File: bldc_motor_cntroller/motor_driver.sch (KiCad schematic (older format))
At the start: 44 parts

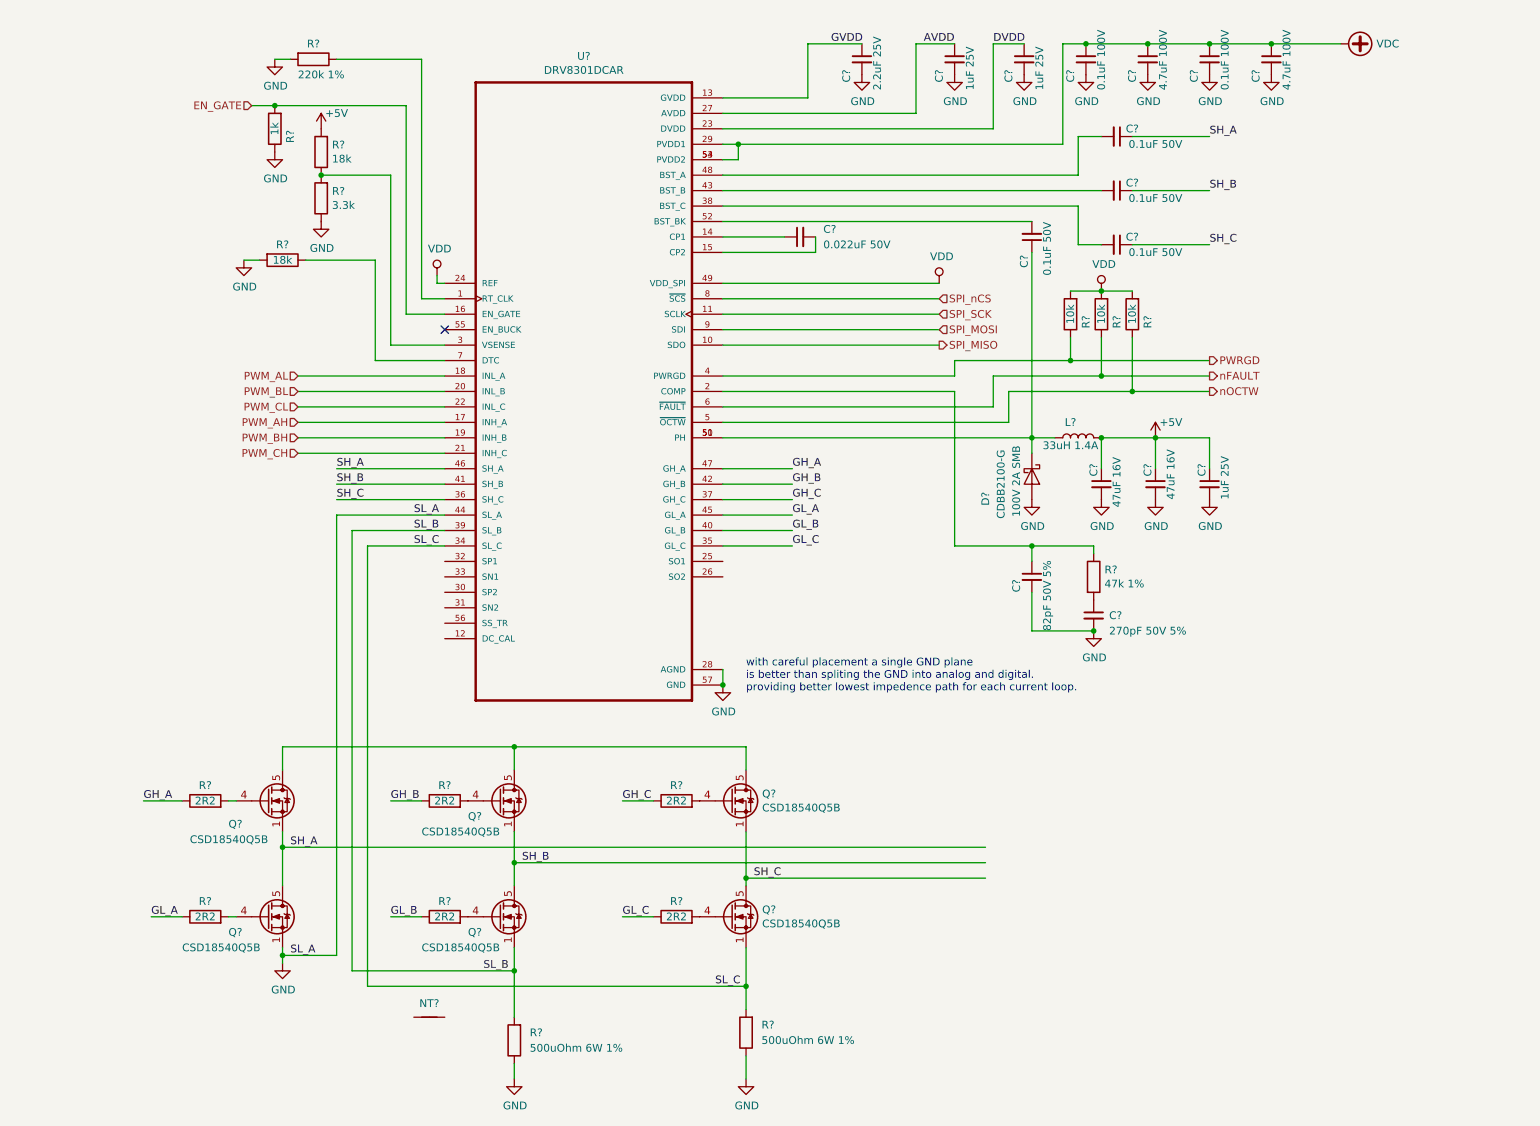
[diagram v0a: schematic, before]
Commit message: finished motor driver interface.
Signed-off-by: azmat bilal <azmat.bilal@outlook.com>
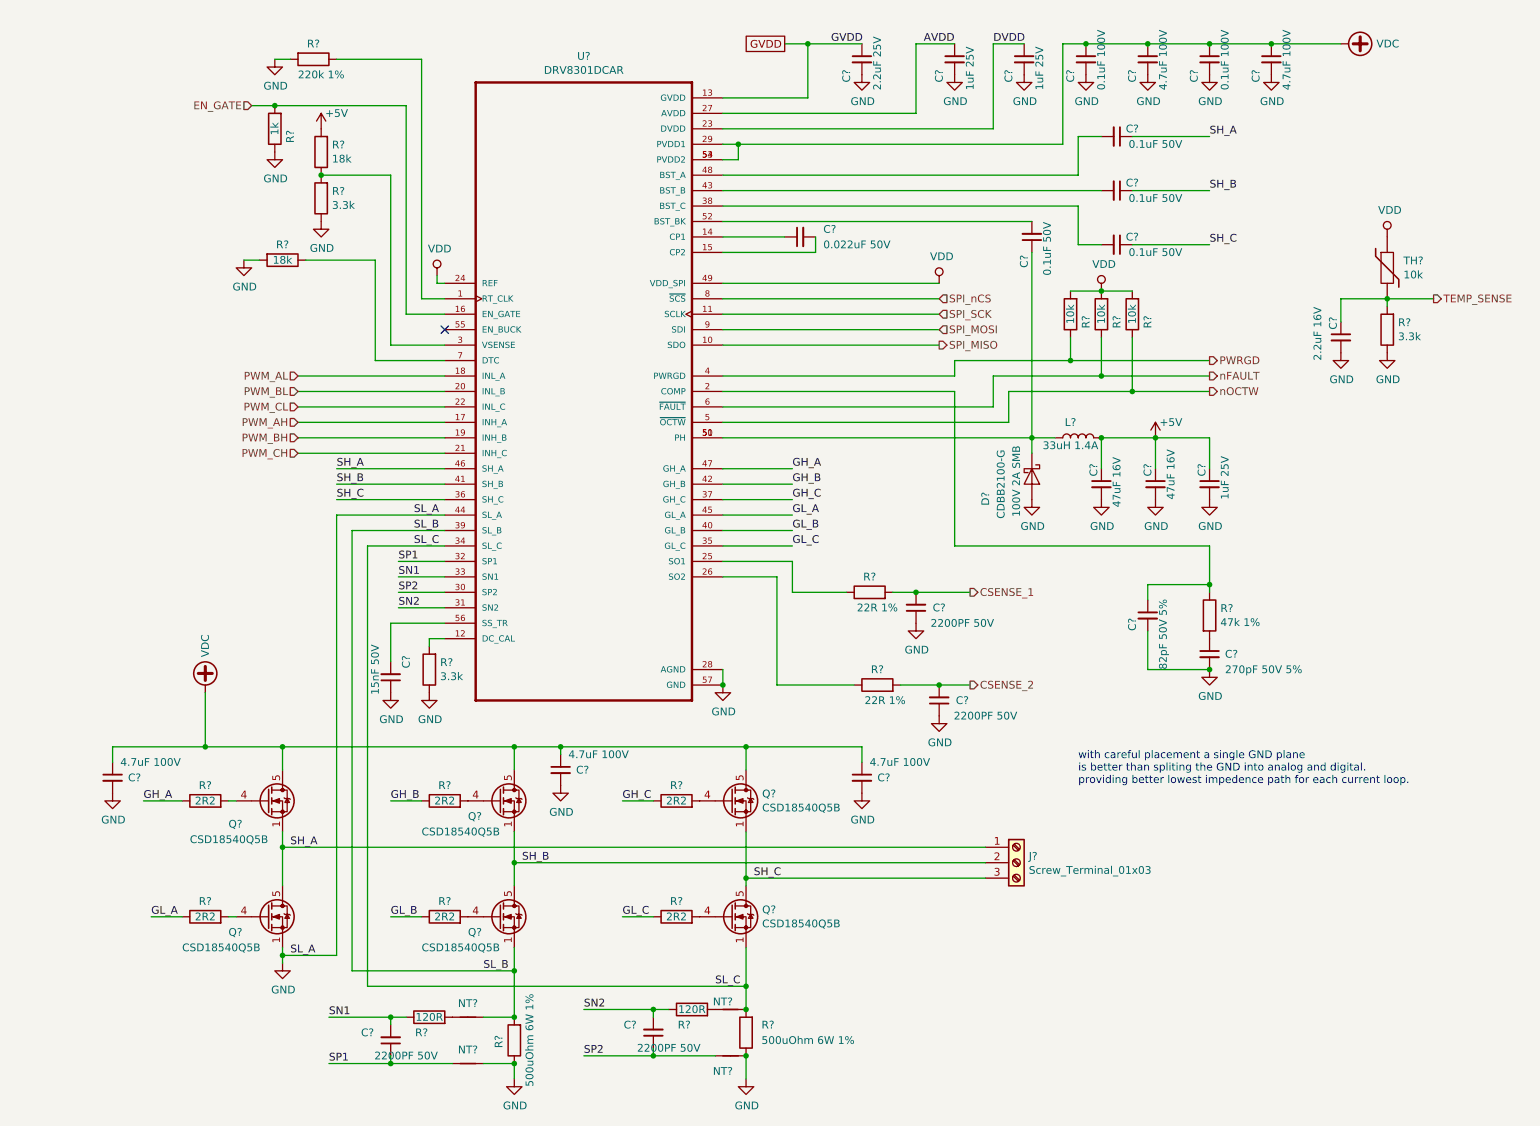
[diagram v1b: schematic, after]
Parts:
- added C? (x4): 2200PF 50V, Capacitor_SMD:C_0402_1005Metric, symbol Device:C_Small
- added C?: 15nF 50V, Capacitor_SMD:C_0402_1005Metric, symbol Device:C_Small
- added C? (x3): 4.7uF 100V, Capacitor_SMD:C_1210_3225Metric, symbol Device:C_Small
- added C?: 2.2uF 16V, Capacitor_SMD:C_0402_1005Metric, symbol Device:C_Small
- added J?: Screw_Terminal_01x03, TerminalBlock:TerminalBlock_bornier-3_P5.08mm, symbol Connector:Screw_Terminal_01x03
- added NT? (x3): Net-Tie_2, NetTie:NetTie-2_SMD_Pad0.5mm, symbol Device:Net-Tie_2
- added R? (x2): 120R, Resistor_SMD:R_0402_1005Metric, symbol Device:R
- added R? (x2): 3.3k, symbol Device:R
- added R? (x2): 22R 1%, Capacitor_SMD:C_0402_1005Metric, symbol Device:R
- added TH?: 10k, Resistor_SMD:R_0402_1005Metric, symbol Device:Thermistor
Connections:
- net GND: now also C?.1, C?.1, C?.1, C?.2, C?.2, C?.2, C?.2, NT?.2, NT?.2, R?.1, R?.1
- net SH_A: now also J?.1 (Pin_1)
- net SH_B: now also J?.2 (Pin_2)
- net SH_C: now also J?.3 (Pin_3)
- net SL_B: now also NT?.2
- net SL_C: now also NT?.2
- net VDC: now also Q?.5 (D), Q?.5 (D), Q?.5 (D), C?.1, C?.1, C?.1
- net VDD: now also TH?.1
- net at U?.12 (DC_CAL): now also R?.2
- net at U?.25 (SO1): now also R?.1
- net at U?.26 (SO2): now also R?.1
- net SP2: now reaches U?.30 (SP2)
- net SP2: now also C?.1, NT?.1
- net SN2: now reaches U?.31 (SN2)
- net SN2: now also C?.2, R?.1
- net SP1: now reaches U?.32 (SP1)
- net SP1: now also C?.1, NT?.1
- net SN1: now reaches U?.33 (SN1)
- net SN1: now also C?.2, R?.1
- net at U?.56 (SS_TR): now also C?.2
- net at NT?.1: now also R?.2
- new net: NT?.1, R?.2
- new net CSENSE_1: C?.2, R?.2
- new net CSENSE_2: C?.2, R?.2
- new net TEMP_SENSE: C?.1, R?.2, TH?.2
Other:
- moved on the sheet: C?, NT?, R?

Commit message: schematic annotation. added bulk caps. moved shunt res to powersheet.
Signed-off-by: azmat bilal <azmat.bilal@outlook.com>
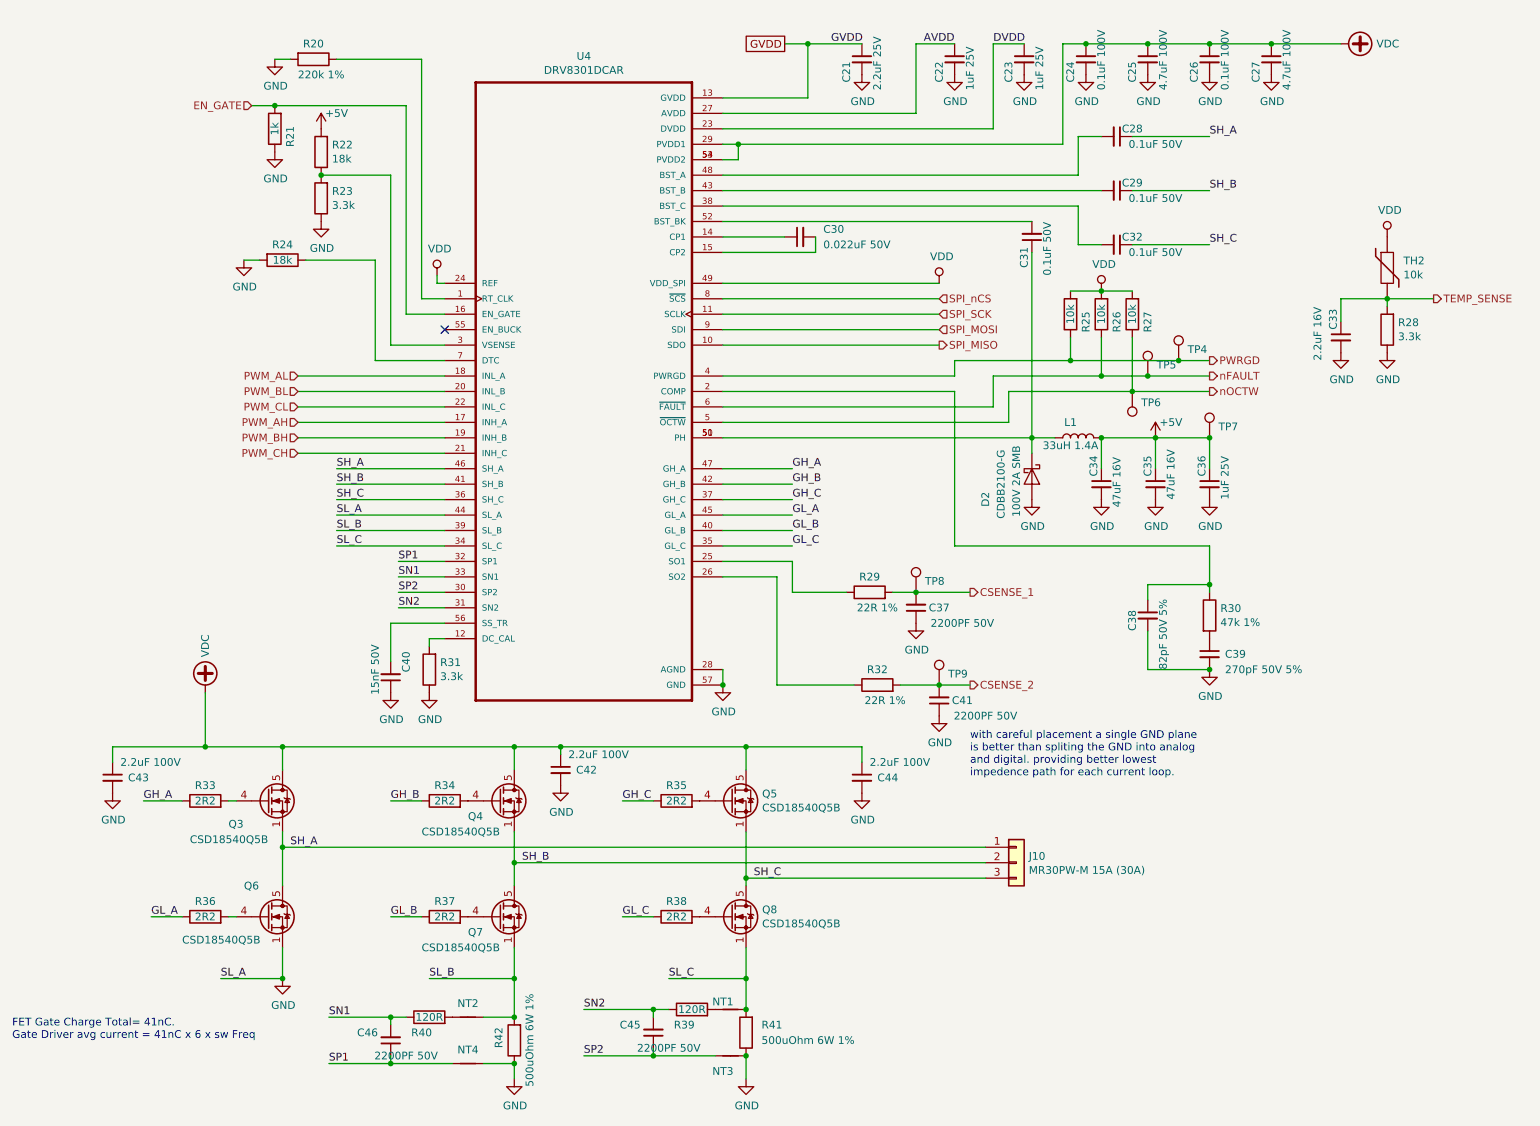
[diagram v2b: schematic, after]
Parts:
- removed J?: Screw_Terminal_01x03, TerminalBlock:TerminalBlock_bornier-3_P5.08mm, symbol Connector:Screw_Terminal_01x03
- added J10: MR30PW-M 15A (30A), Connector_AMASS:AMASS_MR30PW-M_1x03_P3.50mm_Horizontal, symbol Connector_Generic:Conn_01x03
- added TP4, TP5, TP6, TP7, TP8, TP9: TestPoint, symbol Connector:TestPoint
- C42, C43, C44: renamed from C?; value 4.7uF 100V -> 2.2uF 100V
- gave numbers to parts that had none: 60
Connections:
- net +5V: now also TP7.1
- net CSENSE_1: now also TP8.1
- net CSENSE_2: now also TP9.1
- net PWRGD: now also TP4.1
- net SH_A: now also J10.1 (Pin_1)
- net SH_B: now also J10.2 (Pin_2)
- net SH_C: now also J10.3 (Pin_3)
- net nFAULT: now also TP5.1
- net nOCTW: now also TP6.1
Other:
- note added: "FET Gate Charge Total= 41nC.\nGate Driver avg current = 41nC x 6 x sw Freq"
- note added: "with careful placement a single GND plane \nis better than spliting the GND into analog\nand digital. providing better lowest \nimpedence path for each current loop."
- note removed: "with careful placement a single GND plane \nis better than spliting the GND into analog and digital. \nproviding better lowest impedence path for each current loop."

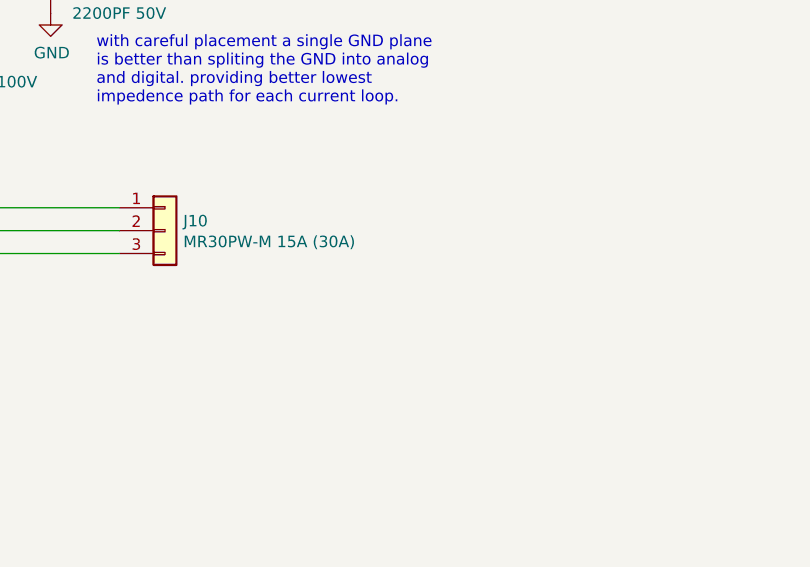
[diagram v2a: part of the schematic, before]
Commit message: added page titles and rev. no.
Signed-off-by: azmat bilal <azmat.bilal@outlook.com>
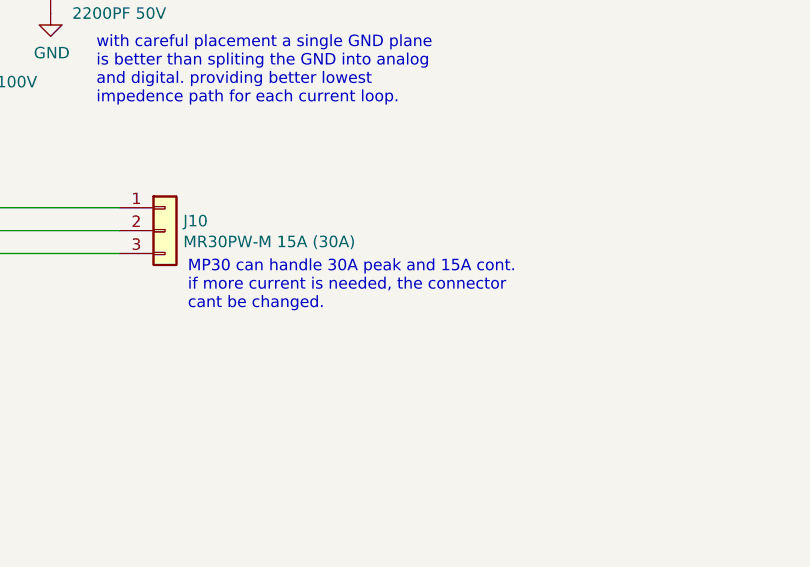
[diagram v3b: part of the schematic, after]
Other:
- note added: "MP30 can handle 30A peak and 15A cont.\nif more current is needed, the connector \ncant be changed."
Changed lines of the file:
@@
 encoding utf-8
 Sheet 4 5
-Title ""
-Date ""
-Rev ""
+Title "Motor Driver"
+Date "2020-01-29"
+Rev "1.0.0"
 Comp ""
 Comment1 ""
@@
 	1    0    0    -1
 $EndComp
+Text Notes 7350 6450 0    50   ~ 0
+MP30 can handle 30A peak and 15A cont.\nif more current is needed, the connector \ncant be changed.
 $EndSCHEMATC

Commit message: added missing footprints.
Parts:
- R20, R21, R22, R23, R24, R25, R26, R27, R28, R30, R31: footprint (none) -> Resistor_SMD:R_0402_1005Metric
- R29, R32, R33, R34, R35, R36, R37, R38: footprint Capacitor_SMD:C_0402_1005Metric -> Resistor_SMD:R_0402_1005Metric
- TP4, TP5, TP6, TP7, TP8, TP9: footprint (none) -> TestPoint:TestPoint_Pad_D1.5mm
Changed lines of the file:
@@
 F 0 "R27" V 7900 2600 50  0000 C CNN
 F 1 "10k" V 8000 2550 50  0000 C CNN
-F 2 "" V 7930 2550 50  0001 C CNN
+F 2 "Resistor_SMD:R_0402_1005Metric" V 7930 2550 50  0001 C CNN
 F 3 "~" H 8000 2550 50  0001 C CNN
 	1    8000 2550
@@
 F 0 "R26" V 7700 2600 50  0000 C CNN
 F 1 "10k" V 7800 2550 50  0000 C CNN
-F 2 "" V 7730 2550 50  0001 C CNN
+F 2 "Resistor_SMD:R_0402_1005Metric" V 7730 2550 50  0001 C CNN
 F 3 "~" H 7800 2550 50  0001 C CNN
 	1    7800 2550
@@
 F 0 "R25" V 7500 2600 50  0000 C CNN
 F 1 "10k" V 7600 2550 50  0000 C CNN
-F 2 "" V 7530 2550 50  0001 C CNN
+F 2 "Resistor_SMD:R_0402_1005Metric" V 7530 2550 50  0001 C CNN
 F 3 "~" H 7600 2550 50  0001 C CNN
 	1    7600 2550
@@
 F 0 "R30" H 8570 4546 50  0000 L CNN
 F 1 "47k 1%" H 8570 4455 50  0000 L CNN
-F 2 "" V 8430 4500 50  0001 C CNN
+F 2 "Resistor_SMD:R_0402_1005Metric" V 8430 4500 50  0001 C CNN
 F 3 "~" H 8500 4500 50  0001 C CNN
 	1    8500 4500
@@
 F 0 "R20" V 2600 900 50  0000 C CNN
 F 1 "220k 1%" V 2800 950 50  0000 C CNN
-F 2 "" V 2630 900 50  0001 C CNN
+F 2 "Resistor_SMD:R_0402_1005Metric" V 2630 900 50  0001 C CNN
 F 3 "~" H 2700 900 50  0001 C CNN
 	1    2700 900
@@
 F 0 "R21" V 2350 1400 50  0000 C CNN
 F 1 "1k" V 2450 1350 50  0000 C CNN
-F 2 "" V 2380 1350 50  0001 C CNN
+F 2 "Resistor_SMD:R_0402_1005Metric" V 2380 1350 50  0001 C CNN
 F 3 "~" H 2450 1350 50  0001 C CNN
 	1    2450 1350
@@
 F 0 "R22" H 2680 1454 50  0000 R CNN
 F 1 "18k" H 2680 1545 50  0000 R CNN
-F 2 "" V 2680 1500 50  0001 C CNN
+F 2 "Resistor_SMD:R_0402_1005Metric" V 2680 1500 50  0001 C CNN
 F 3 "~" H 2750 1500 50  0001 C CNN
 	1    2750 1500
@@
 F 0 "R23" H 2680 1754 50  0000 R CNN
 F 1 "3.3k" H 2680 1845 50  0000 R CNN
-F 2 "" V 2680 1800 50  0001 C CNN
+F 2 "Resistor_SMD:R_0402_1005Metric" V 2680 1800 50  0001 C CNN
 F 3 "~" H 2750 1800 50  0001 C CNN
 	1    2750 1800
@@
 F 0 "R24" V 2400 2200 50  0000 C CNN
 F 1 "18k" V 2500 2200 50  0000 C CNN
-F 2 "" V 2430 2200 50  0001 C CNN
+F 2 "Resistor_SMD:R_0402_1005Metric" V 2430 2200 50  0001 C CNN
 F 3 "~" H 2500 2200 50  0001 C CNN
 	1    2500 2200
@@
 F 0 "R33" V 2100 5700 50  0000 C CNN
 F 1 "2R2" V 2000 5700 50  0000 C CNN
-F 2 "Capacitor_SMD:C_0402_1005Metric" V 1930 5700 50  0001 C CNN
+F 2 "Resistor_SMD:R_0402_1005Metric" V 1930 5700 50  0001 C CNN
 F 3 "~" H 2000 5700 50  0001 C CNN
 	1    2000 5700
@@
 F 0 "R36" V 2100 6450 50  0000 C CNN
 F 1 "2R2" V 2000 6450 50  0000 C CNN
-F 2 "Capacitor_SMD:C_0402_1005Metric" V 1930 6450 50  0001 C CNN
+F 2 "Resistor_SMD:R_0402_1005Metric" V 1930 6450 50  0001 C CNN
 F 3 "~" H 2000 6450 50  0001 C CNN
 	1    2000 6450
@@
 F 0 "R37" V 3650 6450 50  0000 C CNN
 F 1 "2R2" V 3550 6450 50  0000 C CNN
-F 2 "Capacitor_SMD:C_0402_1005Metric" V 3480 6450 50  0001 C CNN
+F 2 "Resistor_SMD:R_0402_1005Metric" V 3480 6450 50  0001 C CNN
 F 3 "~" H 3550 6450 50  0001 C CNN
 	1    3550 6450
@@
 F 0 "R34" V 3650 5700 50  0000 C CNN
 F 1 "2R2" V 3550 5700 50  0000 C CNN
-F 2 "Capacitor_SMD:C_0402_1005Metric" V 3480 5700 50  0001 C CNN
+F 2 "Resistor_SMD:R_0402_1005Metric" V 3480 5700 50  0001 C CNN
 F 3 "~" H 3550 5700 50  0001 C CNN
 	1    3550 5700
@@
 F 0 "R35" V 5150 5700 50  0000 C CNN
 F 1 "2R2" V 5050 5700 50  0000 C CNN
-F 2 "Capacitor_SMD:C_0402_1005Metric" V 4980 5700 50  0001 C CNN
+F 2 "Resistor_SMD:R_0402_1005Metric" V 4980 5700 50  0001 C CNN
 F 3 "~" H 5050 5700 50  0001 C CNN
 	1    5050 5700
@@
 F 0 "R38" V 5150 6450 50  0000 C CNN
 F 1 "2R2" V 5050 6450 50  0000 C CNN
-F 2 "Capacitor_SMD:C_0402_1005Metric" V 4980 6450 50  0001 C CNN
+F 2 "Resistor_SMD:R_0402_1005Metric" V 4980 6450 50  0001 C CNN
 F 3 "~" H 5050 6450 50  0001 C CNN
 	1    5050 6450
@@
 F 0 "R31" H 3380 4804 50  0000 R CNN
 F 1 "3.3k" H 3380 4895 50  0000 R CNN
-F 2 "" V 3380 4850 50  0001 C CNN
+F 2 "Resistor_SMD:R_0402_1005Metric" V 3380 4850 50  0001 C CNN
 F 3 "~" H 3450 4850 50  0001 C CNN
 	1    3450 4850
@@
 F 0 "R29" V 6400 4350 50  0000 C CNN
 F 1 "22R 1%" V 6200 4300 50  0000 C CNN
-F 2 "Capacitor_SMD:C_0402_1005Metric" V 6230 4350 50  0001 C CNN
+F 2 "Resistor_SMD:R_0402_1005Metric" V 6230 4350 50  0001 C CNN
 F 3 "~" H 6300 4350 50  0001 C CNN
 	1    6300 4350
@@
 F 0 "R32" V 6450 4950 50  0000 C CNN
 F 1 "22R 1%" V 6250 4900 50  0000 C CNN
-F 2 "Capacitor_SMD:C_0402_1005Metric" V 6280 4950 50  0001 C CNN
+F 2 "Resistor_SMD:R_0402_1005Metric" V 6280 4950 50  0001 C CNN
 F 3 "~" H 6350 4950 50  0001 C CNN
 	1    6350 4950
@@
 F 0 "R28" H 9580 2604 50  0000 R CNN
 F 1 "3.3k" H 9580 2695 50  0000 R CNN
-F 2 "" V 9580 2650 50  0001 C CNN
+F 2 "Resistor_SMD:R_0402_1005Metric" V 9580 2650 50  0001 C CNN
 F 3 "~" H 9650 2650 50  0001 C CNN
 	1    9650 2650
@@
 F 0 "TP8" H 6658 4422 50  0000 L CNN
 F 1 "TestPoint" H 6658 4377 50  0001 L CNN
-F 2 "" H 6800 4350 50  0001 C CNN
+F 2 "TestPoint:TestPoint_Pad_D1.5mm" H 6800 4350 50  0001 C CNN
 F 3 "~" H 6800 4350 50  0001 C CNN
 	1    6600 4350
@@
 F 0 "TP9" H 6808 5022 50  0000 L CNN
 F 1 "TestPoint" H 6808 4977 50  0001 L CNN
-F 2 "" H 6950 4950 50  0001 C CNN
+F 2 "TestPoint:TestPoint_Pad_D1.5mm" H 6950 4950 50  0001 C CNN
 F 3 "~" H 6950 4950 50  0001 C CNN
 	1    6750 4950
@@
 F 0 "TP7" H 8558 3422 50  0000 L CNN
 F 1 "TestPoint" H 8558 3377 50  0001 L CNN
-F 2 "" H 8700 3350 50  0001 C CNN
+F 2 "TestPoint:TestPoint_Pad_D1.5mm" H 8700 3350 50  0001 C CNN
 F 3 "~" H 8700 3350 50  0001 C CNN
 	1    8500 3350
@@
 F 0 "TP4" H 8358 2922 50  0000 L CNN
 F 1 "TestPoint" H 8358 2877 50  0001 L CNN
-F 2 "" H 8500 2850 50  0001 C CNN
+F 2 "TestPoint:TestPoint_Pad_D1.5mm" H 8500 2850 50  0001 C CNN
 F 3 "~" H 8500 2850 50  0001 C CNN
 	1    8300 2850
@@
 F 0 "TP5" H 8158 3022 50  0000 L CNN
 F 1 "TestPoint" H 8158 2977 50  0001 L CNN
-F 2 "" H 8300 2950 50  0001 C CNN
+F 2 "TestPoint:TestPoint_Pad_D1.5mm" H 8300 2950 50  0001 C CNN
 F 3 "~" H 8300 2950 50  0001 C CNN
 	1    8100 2950
@@
 F 0 "TP6" H 7942 3122 50  0000 R CNN
 F 1 "TestPoint" H 8058 3077 50  0001 L CNN
-F 2 "" H 8200 3050 50  0001 C CNN
+F 2 "TestPoint:TestPoint_Pad_D1.5mm" H 8200 3050 50  0001 C CNN
 F 3 "~" H 8200 3050 50  0001 C CNN
 	1    8000 3050
